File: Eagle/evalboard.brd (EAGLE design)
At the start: 160 x 100.3 mm, 5 parts, among them X1 MAC64L

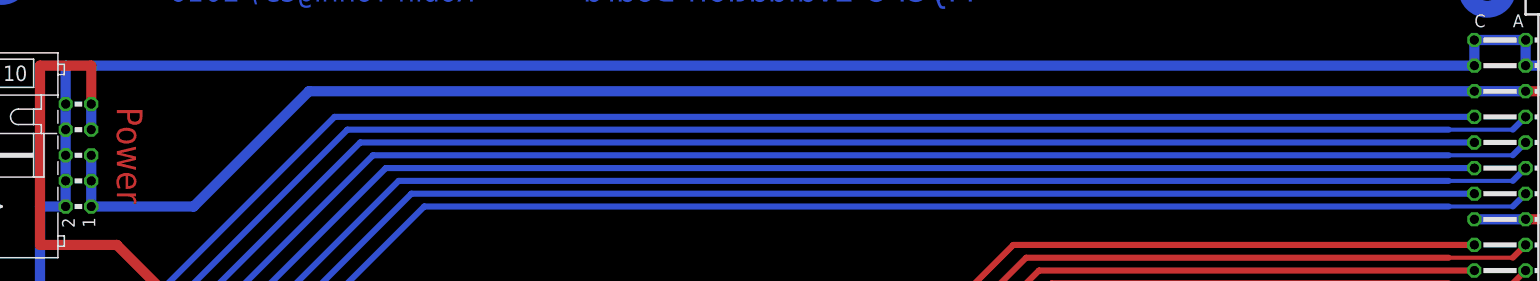
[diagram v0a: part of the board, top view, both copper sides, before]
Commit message: Schematic and layout changes
Added two additional tantal caps for 5V and 12V lines.
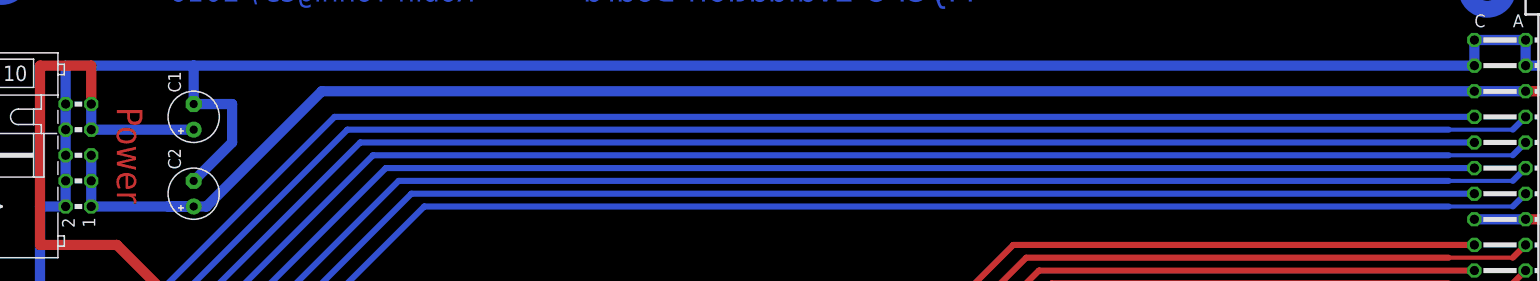
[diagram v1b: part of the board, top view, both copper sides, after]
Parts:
- added C1, C2: 10u, rcl:E2,5-5
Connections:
- net +12V: now also C1.+
- net +5V: now also C2.+
- net GND: now also C1.-, C2.-
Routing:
- net GND: track 292.1 -> 308.9 mm
- net +12V: track 189.2 -> 199.3 mm
- net +5V: track 238.4 -> 241.0 mm
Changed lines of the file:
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@@
 <layer number="24" name="bOrigins" color="15" fill="1" visible="yes" active="yes"/>
 <layer number="25" name="tNames" color="7" fill="1" visible="yes" active="yes"/>
-<layer number="26" name="bNames" color="7" fill="1" visible="yes" active="yes"/>
+<layer number="26" name="bNames" color="7" fill="1" visible="no" active="yes"/>
 <layer number="27" name="tValues" color="7" fill="1" visible="yes" active="yes"/>
 <layer number="28" name="bValues" color="7" fill="1" visible="yes" active="yes"/>
@@
 <layer number="37" name="tTest" color="7" fill="1" visible="no" active="yes"/>
 <layer number="38" name="bTest" color="7" fill="1" visible="no" active="yes"/>
-<layer number="39" name="tKeepout" color="4" fill="11" visible="yes" active="yes"/>
-<layer number="40" name="bKeepout" color="1" fill="11" visible="yes" active="yes"/>
-<layer number="41" name="tRestrict" color="4" fill="10" visible="yes" active="yes"/>
-<layer number="42" name="bRestrict" color="1" fill="10" visible="yes" active="yes"/>
-<layer number="43" name="vRestrict" color="2" fill="10" visible="yes" active="yes"/>
+<layer number="39" name="tKeepout" color="4" fill="11" visible="no" active="yes"/>
+<layer number="40" name="bKeepout" color="1" fill="11" visible="no" active="yes"/>
+<layer number="41" name="tRestrict" color="4" fill="10" visible="no" active="yes"/>
+<layer number="42" name="bRestrict" color="1" fill="10" visible="no" active="yes"/>
+<layer number="43" name="vRestrict" color="2" fill="10" visible="no" active="yes"/>
 <layer number="44" name="Drills" color="7" fill="1" visible="no" active="yes"/>
-<layer number="45" name="Holes" color="7" fill="1" visible="yes" active="yes"/>
+<layer number="45" name="Holes" color="7" fill="1" visible="no" active="yes"/>
 <layer number="46" name="Milling" color="3" fill="1" visible="no" active="yes"/>
 <layer number="47" name="Measures" color="7" fill="1" visible="no" active="yes"/>
-<layer number="48" name="Document" color="7" fill="1" visible="yes" active="yes"/>
-<layer number="49" name="Reference" color="7" fill="1" visible="yes" active="yes"/>
-<layer number="51" name="tDocu" color="7" fill="1" visible="yes" active="yes"/>
-<layer number="52" name="bDocu" color="7" fill="1" visible="yes" active="yes"/>
+<layer number="48" name="Document" color="7" fill="1" visible="no" active="yes"/>
+<layer number="49" name="Reference" color="7" fill="1" visible="no" active="yes"/>
+<layer number="51" name="tDocu" color="7" fill="1" visible="no" active="yes"/>
+<layer number="52" name="bDocu" color="7" fill="1" visible="no" active="yes"/>
 <layer number="90" name="Modules" color="5" fill="1" visible="no" active="no"/>
 <layer number="91" name="Nets" color="2" fill="1" visible="no" active="no"/>
@@
 </element>
 <element name="X1" library="con-vg" package="MAC64L" value="MAC64L" x="157.48" y="49.53"/>
+<element name="C1" library="rcl" package="E2,5-5" value="10u" x="22.86" y="81.28" rot="R90"/>
+<element name="C2" library="rcl" package="E2,5-5" value="10u" x="22.86" y="73.66" rot="R90"/>
 </elements>
 <signals>
@@
 <wire x1="149.86" y1="12.7" x2="149.86" y2="10.16" width="1.016" layer="16"/>
 <wire x1="149.86" y1="10.16" x2="154.94" y2="10.16" width="1.016" layer="16"/>
-<wire x1="149.86" y1="86.36" x2="10.16" y2="86.36" width="1.016" layer="16"/>
+<wire x1="149.86" y1="86.36" x2="22.86" y2="86.36" width="1.016" layer="16"/>
+<wire x1="22.86" y1="86.36" x2="10.16" y2="86.36" width="1.016" layer="16"/>
 <wire x1="10.16" y1="86.36" x2="10.16" y2="82.55" width="1.016" layer="16"/>
+<contactref element="C1" pad="-"/>
+<wire x1="22.86" y1="82.55" x2="22.86" y2="86.36" width="1.016" layer="16"/>
+<contactref element="C2" pad="-"/>
+<wire x1="22.86" y1="74.93" x2="26.67" y2="78.74" width="1.016" layer="16"/>
+<wire x1="26.67" y1="78.74" x2="26.67" y2="82.55" width="1.016" layer="16"/>
+<wire x1="26.67" y1="82.55" x2="22.86" y2="82.55" width="1.016" layer="16"/>
 </signal>
 <signal name="+5V">
@@
 <wire x1="149.86" y1="71.12" x2="154.94" y2="71.12" width="1.016" layer="16"/>
 <wire x1="12.7" y1="72.39" x2="22.86" y2="72.39" width="1.016" layer="16"/>
-<wire x1="22.86" y1="72.39" x2="34.29" y2="83.82" width="1.016" layer="16"/>
-<wire x1="34.29" y1="83.82" x2="149.86" y2="83.82" width="1.016" layer="16"/>
+<contactref element="C2" pad="+"/>
+<wire x1="35.56" y1="83.82" x2="149.86" y2="83.82" width="1.016" layer="16"/>
+<wire x1="22.86" y1="72.39" x2="20.32" y2="72.39" width="1.016" layer="16"/>
+<wire x1="22.86" y1="72.39" x2="24.13" y2="72.39" width="1.016" layer="16"/>
+<wire x1="24.13" y1="72.39" x2="35.56" y2="83.82" width="1.016" layer="16"/>
 </signal>
 <signal name="+12V">
@@
 <wire x1="7.62" y1="86.36" x2="12.7" y2="86.36" width="1.016" layer="1"/>
 <wire x1="12.7" y1="86.36" x2="12.7" y2="82.55" width="1.016" layer="1"/>
+<contactref element="C1" pad="+"/>
+<wire x1="12.7" y1="80.01" x2="22.86" y2="80.01" width="1.016" layer="16"/>
 </signal>
 <signal name="A1">
